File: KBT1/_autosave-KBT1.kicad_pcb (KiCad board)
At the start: 2 copper layers, 33 parts, among them J1 Conn_01x08_Male, K0 KEYSW, K1 KEYSW, K10 KEYSW, K11 KEYSW, K12 KEYSW, K13 KEYSW, K14 KEYSW, K15 KEYSW, K2 KEYSW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

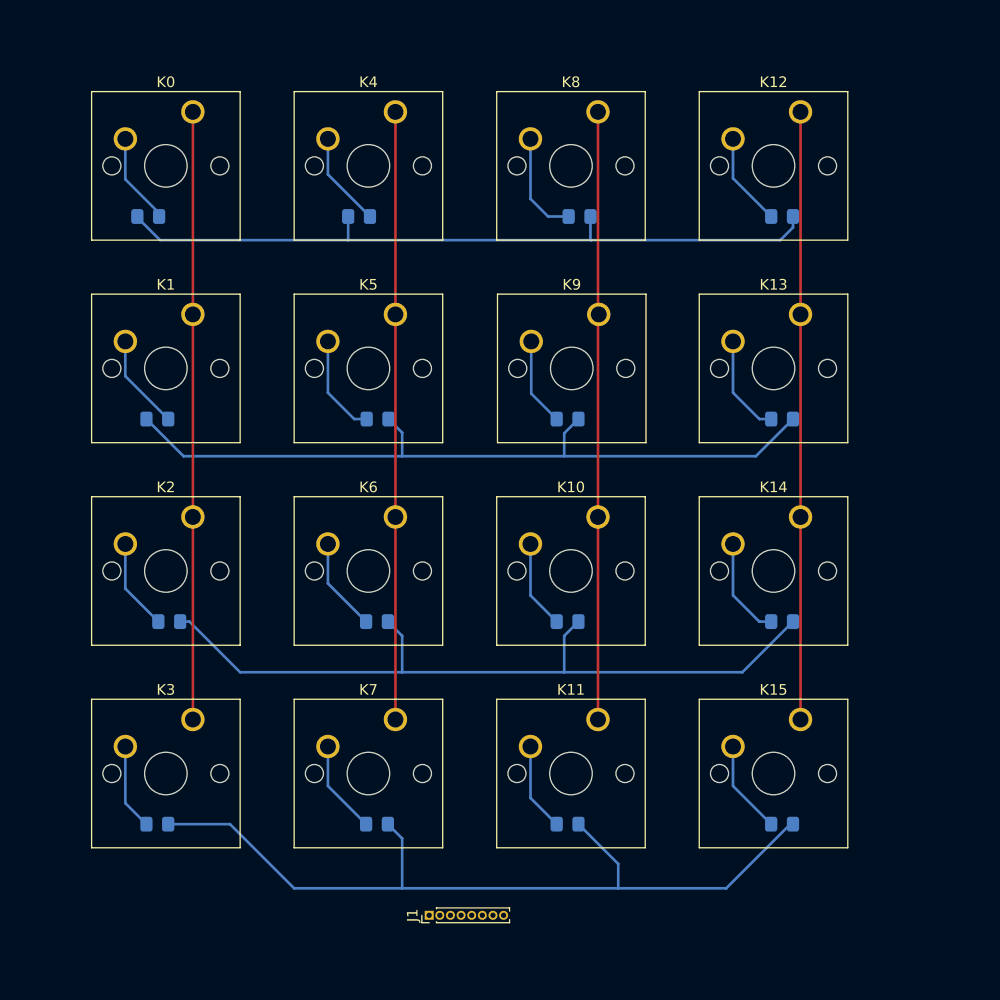
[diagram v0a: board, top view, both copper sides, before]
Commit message: added board outline, added missing trace
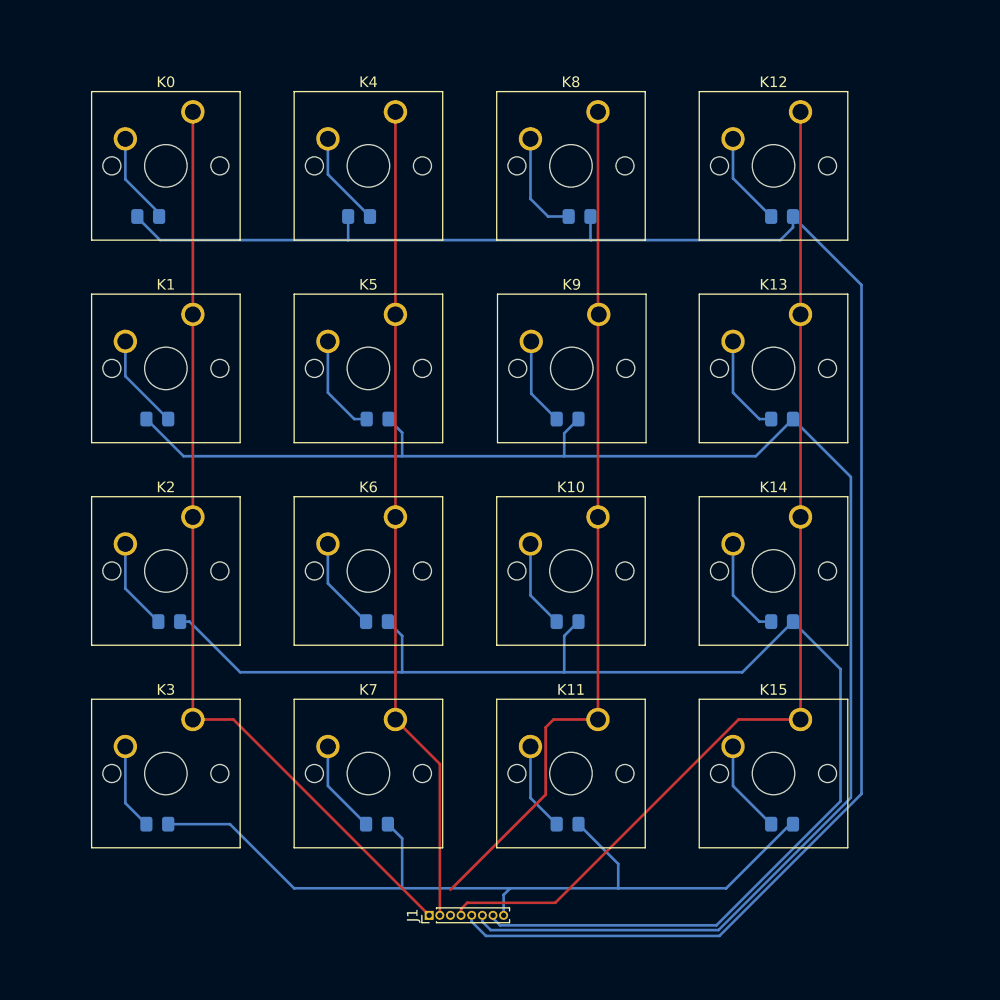
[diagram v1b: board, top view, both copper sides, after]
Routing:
- net /row0: track 68.6 -> 169.0 mm
- net /row1: track 71.8 -> 150.4 mm
- net /row2: track 72.2 -> 129.0 mm
- net /col3: track 58.0 -> 98.0 mm
- net /col0: track 57.1 -> 87.0 mm
- net /col2: track 57.1 -> 81.4 mm
- net /col1: track 57.1 -> 77.3 mm
- net /row3: track 77.9 -> 80.7 mm
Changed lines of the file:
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@@
   (segment (start 45.72 35.56) (end 68.58 35.56) (width 0.25) (layer "B.Cu") (net 2))
   (segment (start 68.58 35.56) (end 86.36 35.56) (width 0.25) (layer "B.Cu") (net 2))
+  (segment (start 57.34 99.66104) (end 58.67896 101) (width 0.25) (layer "B.Cu") (net 2))
   (segment (start 25.89 33.3375) (end 25.89 33.42375) (width 0.25) (layer "B.Cu") (net 2))
+  (segment (start 80.636396 101) (end 94 87.636396) (width 0.25) (layer "B.Cu") (net 2))
   (segment (start 28.02625 35.56) (end 45.72 35.56) (width 0.25) (layer "B.Cu") (net 2))
   (segment (start 25.89 33.42375) (end 28.02625 35.56) (width 0.25) (layer "B.Cu") (net 2))
   (segment (start 87.55625 34.36375) (end 87.55625 33.3375) (width 0.25) (layer "B.Cu") (net 2))
   (segment (start 68.50625 35.48625) (end 68.58 35.56) (width 0.25) (layer "B.Cu") (net 2))
+  (segment (start 57.34 99.06) (end 57.34 99.66104) (width 0.25) (layer "B.Cu") (net 2))
+  (segment (start 94 87.636396) (end 94 39.78125) (width 0.25) (layer "B.Cu") (net 2))
   (segment (start 68.50625 33.3375) (end 68.50625 35.48625) (width 0.25) (layer "B.Cu") (net 2))
   (segment (start 86.36 35.56) (end 87.55625 34.36375) (width 0.25) (layer "B.Cu") (net 2))
   (segment (start 45.72 33.3375) (end 45.72 35.56) (width 0.25) (layer "B.Cu") (net 2))
+  (segment (start 94 39.78125) (end 87.55625 33.3375) (width 0.25) (layer "B.Cu") (net 2))
+  (segment (start 58.67896 101) (end 80.636396 101) (width 0.25) (layer "B.Cu") (net 2))
   (segment (start 24.765 48.35875) (end 24.765 45.085) (width 0.25) (layer "B.Cu") (net 3))
   (segment (start 28.79375 52.3875) (end 24.765 48.35875) (width 0.25) (layer "B.Cu") (net 3))
@@
   (segment (start 49.5125 52.3875) (end 50.8 53.675) (width 0.25) (layer "B.Cu") (net 4))
   (segment (start 87.55625 52.3875) (end 84.06375 55.88) (width 0.25) (layer "B.Cu") (net 4))
+  (segment (start 59.12896 100.45) (end 80.55 100.45) (width 0.25) (layer "B.Cu") (net 4))
   (segment (start 50.8 53.675) (end 50.8 55.88) (width 0.25) (layer "B.Cu") (net 4))
+  (segment (start 58.34 99.06) (end 58.34 99.66104) (width 0.25) (layer "B.Cu") (net 4))
+  (segment (start 93 57.83125) (end 87.55625 52.3875) (width 0.25) (layer "B.Cu") (net 4))
   (segment (start 67.38125 52.3875) (end 66.04 53.72875) (width 0.25) (layer "B.Cu") (net 4))
   (segment (start 84.06375 55.88) (end 30.23625 55.88) (width 0.25) (layer "B.Cu") (net 4))
+  (segment (start 93 88) (end 93 57.83125) (width 0.25) (layer "B.Cu") (net 4))
+  (segment (start 80.55 100.45) (end 93 88) (width 0.25) (layer "B.Cu") (net 4))
   (segment (start 66.04 53.72875) (end 66.04 55.88) (width 0.25) (layer "B.Cu") (net 4))
+  (segment (start 58.34 99.66104) (end 59.12896 100.45) (width 0.25) (layer "B.Cu") (net 4))
   (segment (start 24.765 68.33375) (end 24.765 64.135) (width 0.25) (layer "B.Cu") (net 5))
   (segment (start 27.86875 71.4375) (end 24.765 68.33375) (width 0.25) (layer "B.Cu") (net 5))
+  (segment (start 80.363604 100) (end 92.030001 88.333603) (width 0.25) (layer "B.Cu") (net 6))
+  (segment (start 59.34 99.34) (end 60 100) (width 0.25) (layer "B.Cu") (net 6))
   (segment (start 49.45625 71.4375) (end 50.8 72.78125) (width 0.25) (layer "B.Cu") (net 6))
   (segment (start 67.38125 71.4375) (end 66.04 72.77875) (width 0.25) (layer "B.Cu") (net 6))
   (segment (start 66.04 72.77875) (end 66.04 76.2) (width 0.25) (layer "B.Cu") (net 6))
   (segment (start 35.56 76.2) (end 82.79375 76.2) (width 0.25) (layer "B.Cu") (net 6))
+  (segment (start 92.030001 75.911251) (end 87.55625 71.4375) (width 0.25) (layer "B.Cu") (net 6))
   (segment (start 82.79375 76.2) (end 87.55625 71.4375) (width 0.25) (layer "B.Cu") (net 6))
+  (segment (start 92.030001 88.333603) (end 92.030001 75.911251) (width 0.25) (layer "B.Cu") (net 6))
   (segment (start 30.7975 71.4375) (end 35.56 76.2) (width 0.25) (layer "B.Cu") (net 6))
+  (segment (start 59.34 99.06) (end 59.34 99.34) (width 0.25) (layer "B.Cu") (net 6))
+  (segment (start 60 100) (end 80.363604 100) (width 0.25) (layer "B.Cu") (net 6))
   (segment (start 50.8 72.78125) (end 50.8 76.2) (width 0.25) (layer "B.Cu") (net 6))
   (segment (start 29.91875 71.4375) (end 30.7975 71.4375) (width 0.25) (layer "B.Cu") (net 6))
   (segment (start 24.765 83.185) (end 24.765 88.50875) (width 0.25) (layer "B.Cu") (net 7))
   (segment (start 24.765 88.50875) (end 26.74375 90.4875) (width 0.25) (layer "B.Cu") (net 7))
-  (segment (start 81.28 96.52) (end 40.64 96.52) (width 0.25) (layer "B.Cu") (net 8))
   (segment (start 87.3125 90.4875) (end 81.28 96.52) (width 0.25) (layer "B.Cu") (net 8))
   (segment (start 50.8 91.83125) (end 50.8 96.52) (width 0.25) (layer "B.Cu") (net 8))
@@
   (segment (start 49.45625 90.4875) (end 50.8 91.83125) (width 0.25) (layer "B.Cu") (net 8))
   (segment (start 71.12 94.22625) (end 71.12 96.52) (width 0.25) (layer "B.Cu") (net 8))
+  (segment (start 81.28 96.52) (end 60.96 96.52) (width 0.25) (layer "B.Cu") (net 8))
+  (segment (start 60.96 96.52) (end 40.64 96.52) (width 0.25) (layer "B.Cu") (net 8))
+  (segment (start 60.34 99.06) (end 60.34 97.14) (width 0.25) (layer "B.Cu") (net 8))
+  (segment (start 60.34 97.14) (end 60.96 96.52) (width 0.25) (layer "B.Cu") (net 8))
   (segment (start 34.6075 90.4875) (end 28.79375 90.4875) (width 0.25) (layer "B.Cu") (net 8))
   (segment (start 47.77 33.3375) (end 43.815 29.3825) (width 0.25) (layer "B.Cu") (net 9))
@@
   (segment (start 81.915 86.89625) (end 81.915 83.185) (width 0.25) (layer "B.Cu") (net 20))
   (segment (start 85.50625 90.4875) (end 81.915 86.89625) (width 0.25) (layer "B.Cu") (net 20))
+  (segment (start 34.925 80.645) (end 53.34 99.06) (width 0.25) (layer "F.Cu") (net 21))
+  (segment (start 31.115 80.645) (end 34.925 80.645) (width 0.25) (layer "F.Cu") (net 21))
   (segment (start 31.115 23.495) (end 31.115 80.645) (width 0.25) (layer "F.Cu") (net 21))
   (segment (start 50.165 23.495) (end 50.165 80.645) (width 0.25) (layer "F.Cu") (net 22))
+  (segment (start 54.34 84.82) (end 54.34 99.06) (width 0.25) (layer "F.Cu") (net 22))
+  (segment (start 50.165 80.645) (end 54.34 84.82) (width 0.25) (layer "F.Cu") (net 22))
+  (segment (start 65.037484 80.645) (end 64.299999 81.382485) (width 0.25) (layer "F.Cu") (net 23))
   (segment (start 69.215 23.495) (end 69.215 80.645) (width 0.25) (layer "F.Cu") (net 23))
+  (segment (start 64.299999 87.700001) (end 55.34 96.66) (width 0.25) (layer "F.Cu") (net 23))
+  (segment (start 64.299999 81.382485) (end 64.299999 87.700001) (width 0.25) (layer "F.Cu") (net 23))
+  (segment (start 69.215 80.645) (end 65.037484 80.645) (width 0.25) (layer "F.Cu") (net 23))
+  (segment (start 88.265 80.645) (end 82.439745 80.645) (width 0.25) (layer "F.Cu") (net 24))
+  (segment (start 56.918296 97.880664) (end 56.34 98.45896) (width 0.25) (layer "F.Cu") (net 24))
   (segment (start 88.265 23.495) (end 88.9 22.86) (width 0.25) (layer "F.Cu") (net 24))
   (segment (start 88.265 23.495) (end 88.265 80.645) (width 0.25) (layer "F.Cu") (net 24))
+  (segment (start 56.34 98.45896) (end 56.34 99.06) (width 0.25) (layer "F.Cu") (net 24))
+  (segment (start 82.439745 80.645) (end 65.204081 97.880664) (width 0.25) (layer "F.Cu") (net 24))
+  (segment (start 65.204081 97.880664) (end 56.918296 97.880664) (width 0.25) (layer "F.Cu") (net 24))
 )

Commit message: increased header size
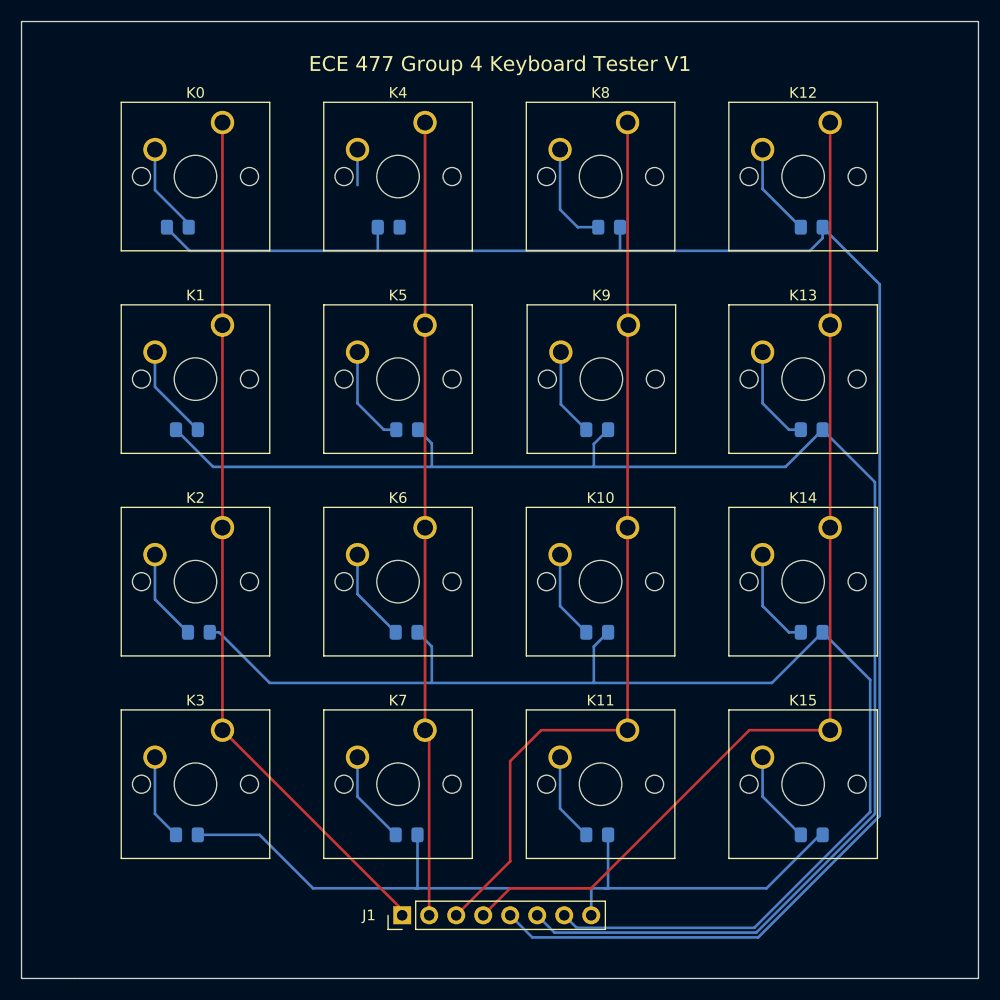
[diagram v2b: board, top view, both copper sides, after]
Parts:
- J1: footprint Connector_PinHeader_1.00mm:PinHeader_1x08_P1.00mm_Vertical -> Connector_PinHeader_2.54mm:PinHeader_1x08_P2.54mm_Vertical
- moved D8 2.96 mm to (51.2, 91.5)
- moved K7 2.96 mm to (53.0, 81.7)
- moved D5 2.96 mm to (49.5, 34.3)
- moved K6 2.96 mm to (53.0, 62.6)
- moved K4 2.96 mm to (53.0, 24.5)
- moved D4 2.96 mm to (30.6, 91.5)
- moved K3 2.96 mm to (33.9, 81.7)
- moved D6 2.96 mm to (51.3, 53.4)
- moved D7 2.96 mm to (51.2, 72.4)
- moved K5 2.96 mm to (53.0, 43.5)
- moved D1 2.96 mm to (29.7, 34.3)
- moved K2 2.96 mm to (33.9, 62.6)
- moved D12 2.96 mm to (69.1, 91.5)
- moved D16 2.96 mm to (89.3, 91.5)
- moved K0 2.96 mm to (33.9, 24.5)
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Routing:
- net Net-(D5-Pad2): track 9.84 -> 4.25 mm
- net /col0: track 87.0 -> 81.6 mm
- net /row3: track 80.7 -> 76.0 mm
- net /col2: track 81.4 -> 86.0 mm
- net /row2: track 129.0 -> 124.7 mm
- net /row1: track 150.4 -> 147.0 mm
- net /col1: track 77.3 -> 74.7 mm
- net /row0: track 169.0 -> 166.6 mm
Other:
- board outline added: 90 x 90 mm
- board text added: "ECE 477 Group 4 Keyboard Tester V1"
